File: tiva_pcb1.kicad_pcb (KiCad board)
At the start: 4 copper layers, 50 x 50 mm, 57 parts, among them K1 CONN_3, P1 CONN_5X2, P2 CONN_5X2, P3 CONN_5X2, P4 MICRO-SD, P5 CONN_2, P6 CONN_3, P7 CONN_4X2, P8 CONN_9, P9 CONN_3X2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

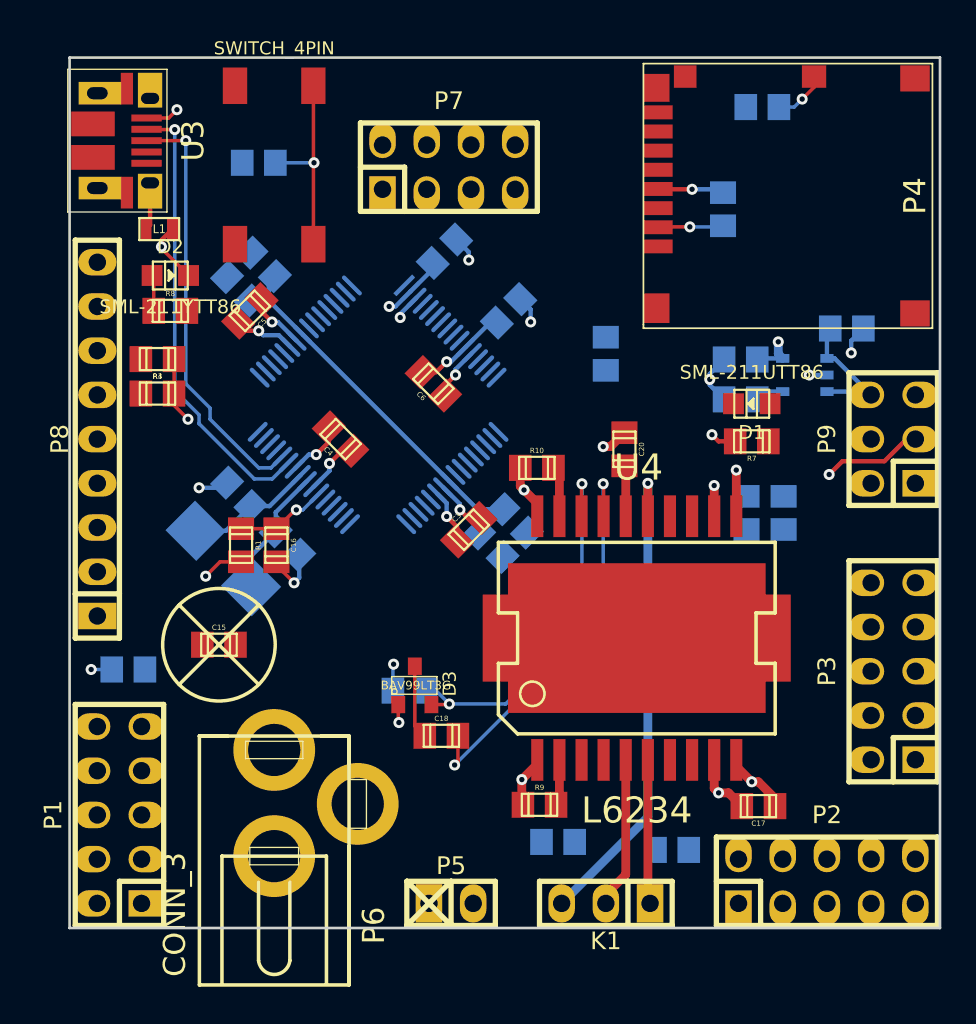
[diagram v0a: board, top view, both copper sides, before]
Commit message: Tweak a couple of things, in preparation for another autoroute attempt:
 - Fix position of the connectors around the edge of the board.
 - Proper ground plane zone fill.
 - Move USB data lines a bit to make more routing space.
 - Re-route the +3.3V along the top of the board to make more space for
   routing below where there are more signals.
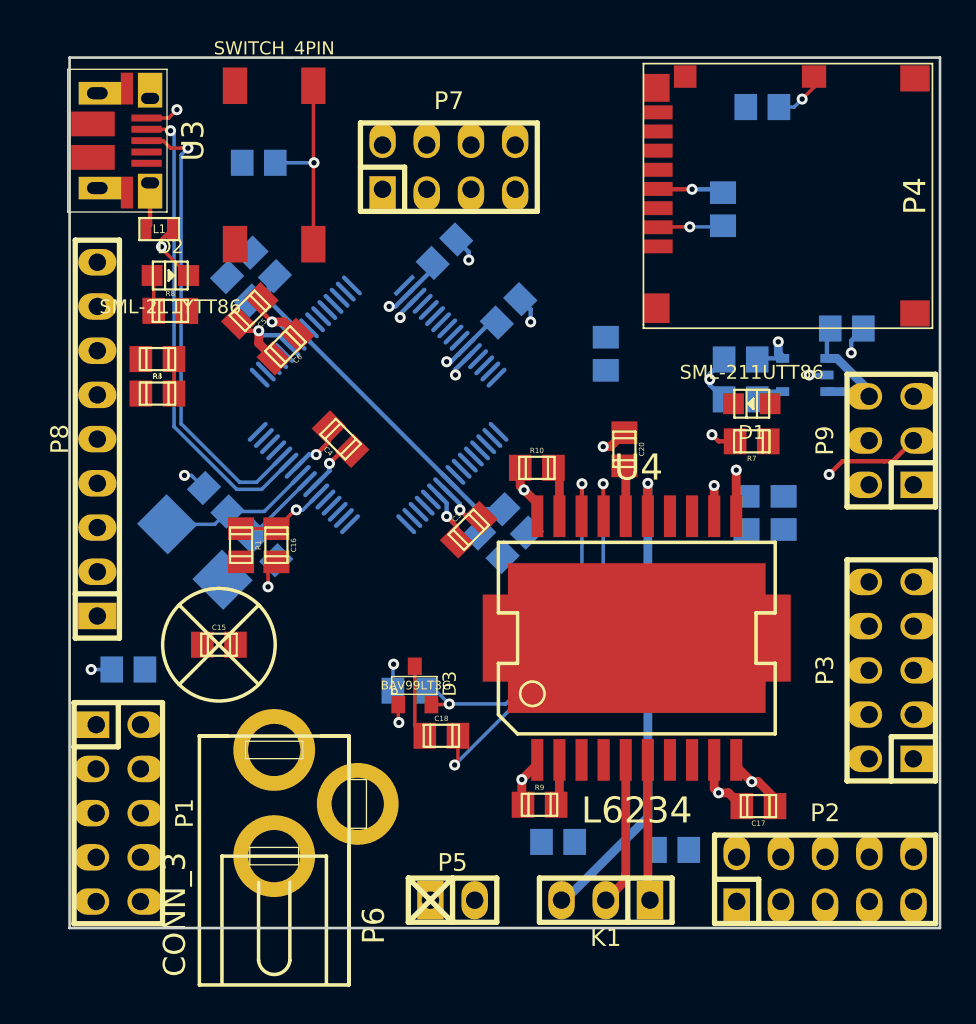
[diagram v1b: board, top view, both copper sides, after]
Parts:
- moved C6 8.76 mm to (72.4, 76.6), turned to 225 degrees
- moved X1 1.68 mm to (67.2, 88.4)
- moved C7 1.36 mm to (68.4, 85.4)
- moved C8 1.35 mm to (71.2, 88.2)
- moved P5 0.20 mm to (82.0, 108.4)
- moved K1 0.19 mm to (90.8, 108.4)
- moved P2 0.16 mm to (103.4, 107.2)
- moved P9 0.14 mm to (107.2, 82.0)
- moved P3 0.13 mm to (107.2, 95.2)
- moved P1 0.12 mm to (62.8, 103.4), turned to 270 degrees
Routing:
- net /vbat: track 77.6 -> 96.2 mm
- net Net-(C8-Pad1): track 7.37 -> 4.49 mm
- net /usb_dp: track 24.4 -> 26.4 mm
- net Net-(C7-Pad1): track 7.37 -> 8.85 mm
- net /usb_dm: track 25.9 -> 27.2 mm
- net +3.3V: track 138.8 -> 137.5 mm, vias 11 -> 9
- net /usb5v: track 56.8 -> 57.5 mm
- net /hall1: track 0.00 -> 0.61 mm
- added copper zone on Inner2.Cu, net GND

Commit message: First complete version.
Everything routed, DRC passes. Silk screen done, gerbers checked briefly.
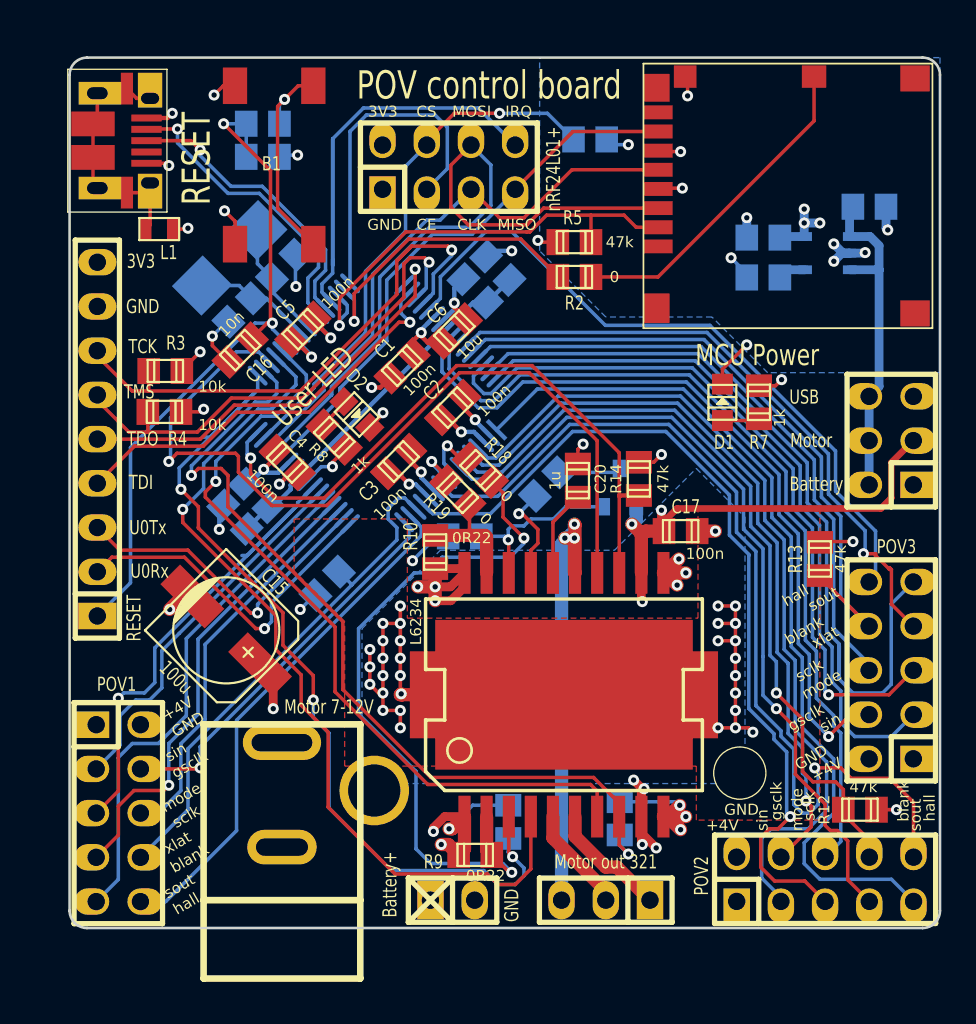
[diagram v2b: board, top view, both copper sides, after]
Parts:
- added 1PIN_6mm: P***, iut:1PIN_6mm, F.Cu at (98.5, 101.1)
- added R17: 47k, w_smd_resistors:r_0805, B.Cu at (89.9, 64.7)
- added R18: 0, w_smd_resistors:r_0805, F.Cu at (83.6, 83.7)
- added R19: 0, w_smd_resistors:r_0805, F.Cu at (82.3, 85.0)
- C1, C2, R12, R13, R14, R2, R5: moved to F.Cu
- C15: footprint w_smd_cap:c_0805 -> w_smd_cap:c_elec_6.3x5.3
- C18, D3, R1: moved to B.Cu
- C6: value 1u -> 10u
- P6: footprint knielsenlib:con-jack-DCJ0303 -> w_conn_misc:dc_socket
- R10, R9: value 0R5 -> 0R22
- R6: value 470 -> 100
- moved R1 22.3 mm to (71.1, 65.7), turned to 0 degrees
- moved R12 18.2 mm to (105.4, 103.2), turned to 180 degrees
- moved X1 17.0 mm to (69.2, 71.5), turned to 225 degrees
- moved C17 16.4 mm to (95.1, 87.2)
- moved D3 16.4 mm to (91.6, 84.7), turned to 180 degrees
- moved C11 16.1 mm to (69.5, 86.4), turned to 315 degrees
- moved C18 15.7 mm to (87.4, 84.5), turned to 225 degrees
- moved R2 14.6 mm to (89.0, 72.6), turned to 180 degrees
- moved C7 14.0 mm to (72.3, 72.0), turned to 225 degrees
- moved C8 13.8 mm to (69.8, 74.5), turned to 45 degrees
- moved C9 13.8 mm to (70.8, 85.2), turned to 315 degrees
- moved C10 13.6 mm to (83.3, 73.4)
- moved C12 13.5 mm to (84.6, 72.1)
- moved D2 13.4 mm to (76.5, 80.5), turned to 315 degrees
- moved R11 12.5 mm to (74.8, 90.2), turned to 45 degrees
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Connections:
- net Net-(C10-Pad1) renamed /vdcc
- net Net-(C18-Pad1) renamed /vcp
- net Net-(C19-Pad1) renamed /vboot
- net Net-(C20-Pad1) renamed /vref
- P6 pad 1: +12V -> Net-(P6-Pad1)
- P6 pad 2: Net-(P6-Pad2) -> GND
- P6 pad 3: GND -> +12V
- R10 pad 1: /m_sense2 -> /m_sense2_raw
- R2 pad 1: /sd_cd -> /sd_cd2
- R2 pad 2: /sd_cd2 -> /sd_cd
- R9 pad 1: /m_sense1 -> /m_sense1_raw
- U1 pad 10: /pd7 -> /hall2
- U1 pad 13: /sd_cd2 -> /mode2
- U1 pad 14: /hall3 -> /blank1
- U1 pad 15: /hall2 -> /hall1
- U1 pad 16: /hall1 -> /gsclk1
- U1 pad 20: /user_led -> /xlat1
- U1 pad 23: /xlat1 -> /mode1
- U1 pad 24: /mode1 -> /user_led
- U1 pad 45: /nrf_ce -> /nrf_irq
- U1 pad 46: /gsclk1 -> /sd_cs
- U1 pad 47: /gsclk2 -> /sd_cd2
- U1 pad 48: /gsclk3 -> /nrf_ce
- U1 pad 5: /nrf_irq -> /gsclk2
- U1 pad 53: /xlat2 -> /hall3
- U1 pad 57: /m_sense1 -> /gsclk3
- U1 pad 59: /blank2 -> /xlat3
- U1 pad 6: /mode3 -> /blank2
- U1 pad 62: /m_sense2 -> /mode3
- U1 pad 7: /xlat3 -> /xlat2
- U1 pad 8: /blank1 -> /m_sense1
- U1 pad 9: /mode2 -> /m_sense2
- U4 pad 19: /m_sense2 -> /m_sense2_raw
- U4 pad 2: /m_sense1 -> /m_sense1_raw
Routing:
- net GND: track 47.7 -> 351.0 mm, vias 19 -> 71
- net /hall2: track 0.00 -> 53.8 mm, vias 0 -> 1
- net /m_en2: track 0.00 -> 52.6 mm, vias 0 -> 3
- net /sout2: track 0.00 -> 50.4 mm
- net /m_in2: track 0.00 -> 49.8 mm, vias 0 -> 1
- net /mode2: track 0.00 -> 49.7 mm, vias 0 -> 1
- net /m_en1: track 0.00 -> 49.3 mm, vias 0 -> 2
- net /sin2: track 0.00 -> 49.1 mm
- net /m_in3: track 0.00 -> 49.1 mm, vias 0 -> 1
- net /sclk2: track 0.00 -> 48.7 mm
- net +3.3V: track 137.5 -> 186.1 mm, vias 9 -> 18
- net /sout3: track 0.00 -> 47.0 mm
- net /xlat2: track 0.00 -> 46.7 mm, vias 0 -> 1
- net /m_in1: track 0.00 -> 45.0 mm, vias 0 -> 1
- net /blank2: track 0.00 -> 44.8 mm, vias 0 -> 1
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- added copper zone on Inner2.Cu, net +12V
- added copper zone on Inner2.Cu, net +3.3V
- added copper zone on Inner2.Cu, net /vbat
- added copper zone on B.Cu, net GND
- added copper zone on F.Cu, net GND
- added copper zone on Inner1.Cu, net GND
- removed copper zone on Inner2.Cu, net GND
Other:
- outline, holes or cut-outs redrawn
- board text added: "+4V"
- board text added: "3V3"
- board text added: "Battery"
- board text added: "Battery+"
- board text added: "CE"
- board text added: "CLK"
- board text added: "CS"
- board text added: "Debug"
- board text added: "GND"
- board text added: "IRQ"
- board text added: "LED power"
- board text added: "MCU Power"
- board text added: "MCU Power select"
- board text added: "MISO"
- board text added: "MOSI"
- board text added: "Motor"
- board text added: "Motor 7-12V"
- board text added: "Motor out"
- board text added: "Motor out 321"
- board text added: "Motor power"
- board text added: "POV control board"
- board text added: "POV wing 1"
- board text added: "POV wing 2"
- board text added: "POV wing 3"
- board text added: "POV1"
- board text added: "POV2"
- board text added: "POV3"
- board text added: "RESET"
- board text added: "TCK"
- board text added: "TDI"
- board text added: "TDO"
- board text added: "TMS"
- board text added: "U0Rx"
- board text added: "U0Tx"
- board text added: "USB"
- board text added: "User LED"
- board text added: "blank"
- board text added: "gsclk"
- board text added: "hall"
- board text added: "knielsen 2013 rev1"
- board text added: "mode"
- board text added: "nRF24L01+"
- board text added: "nRF24L01+ wireless"
- board text added: "sclk"
- board text added: "sin"
- board text added: "sout"
- board text added: "xlat"
